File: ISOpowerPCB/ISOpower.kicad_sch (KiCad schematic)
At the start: 12 parts

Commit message: modified pcb files
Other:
- sheet MCU ports: added ADC0, ADC1, ADC2, ADC3, ADC4, ADC5; removed none

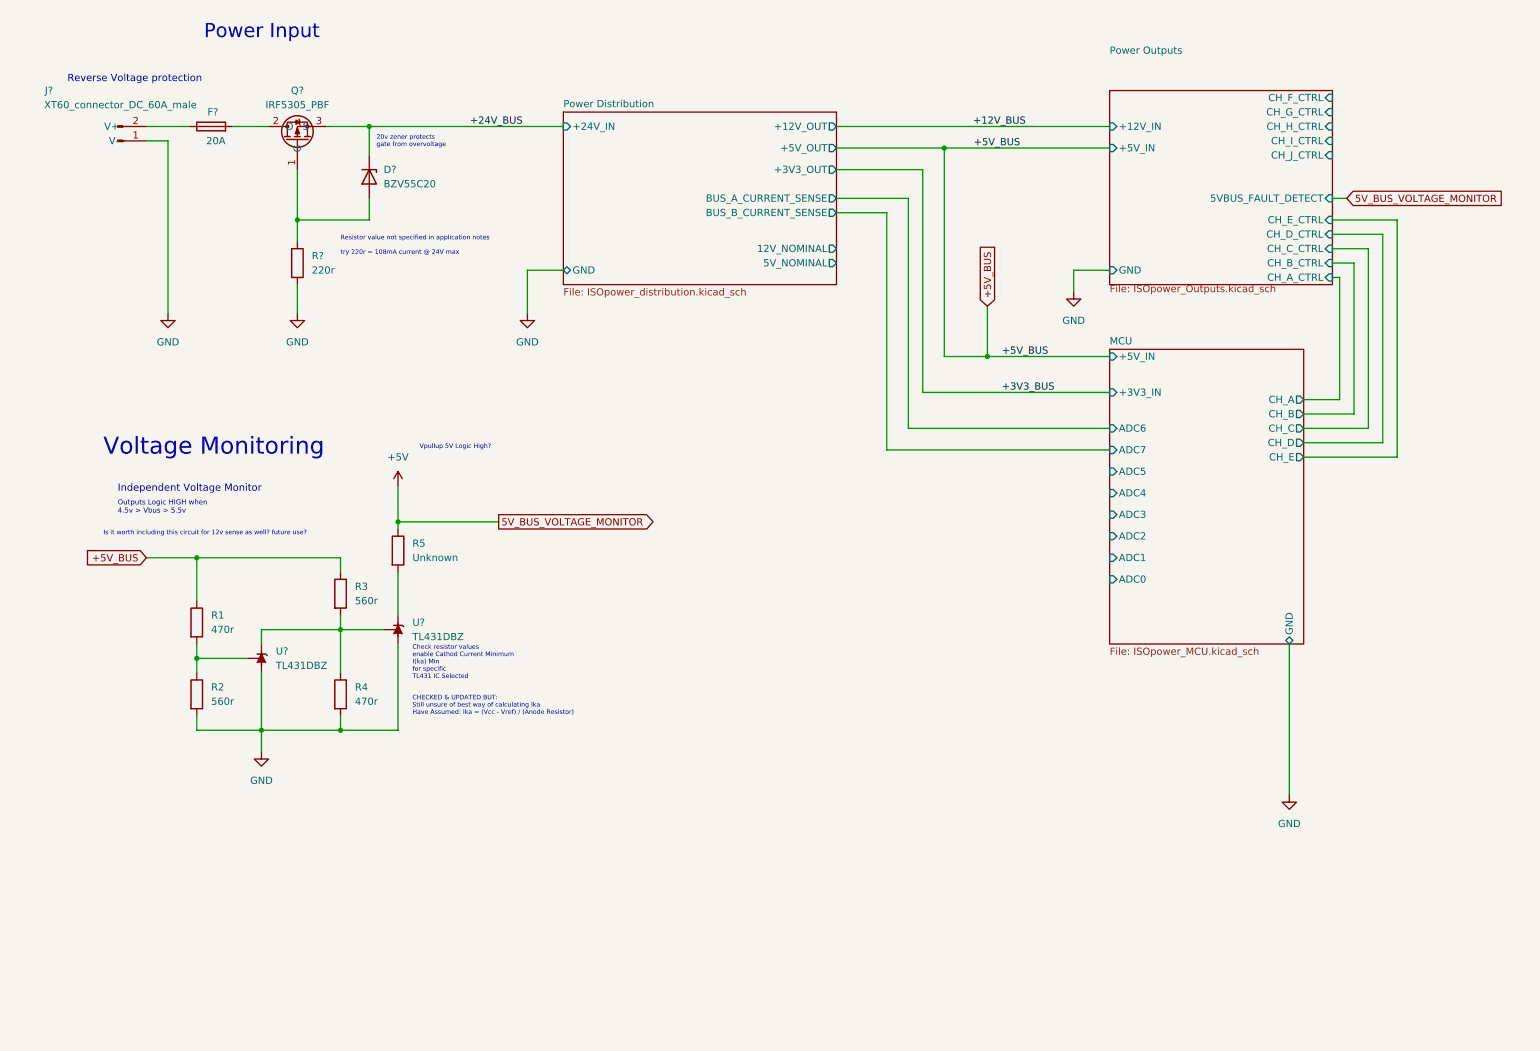
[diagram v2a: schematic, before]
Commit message: Finished initial circuit design
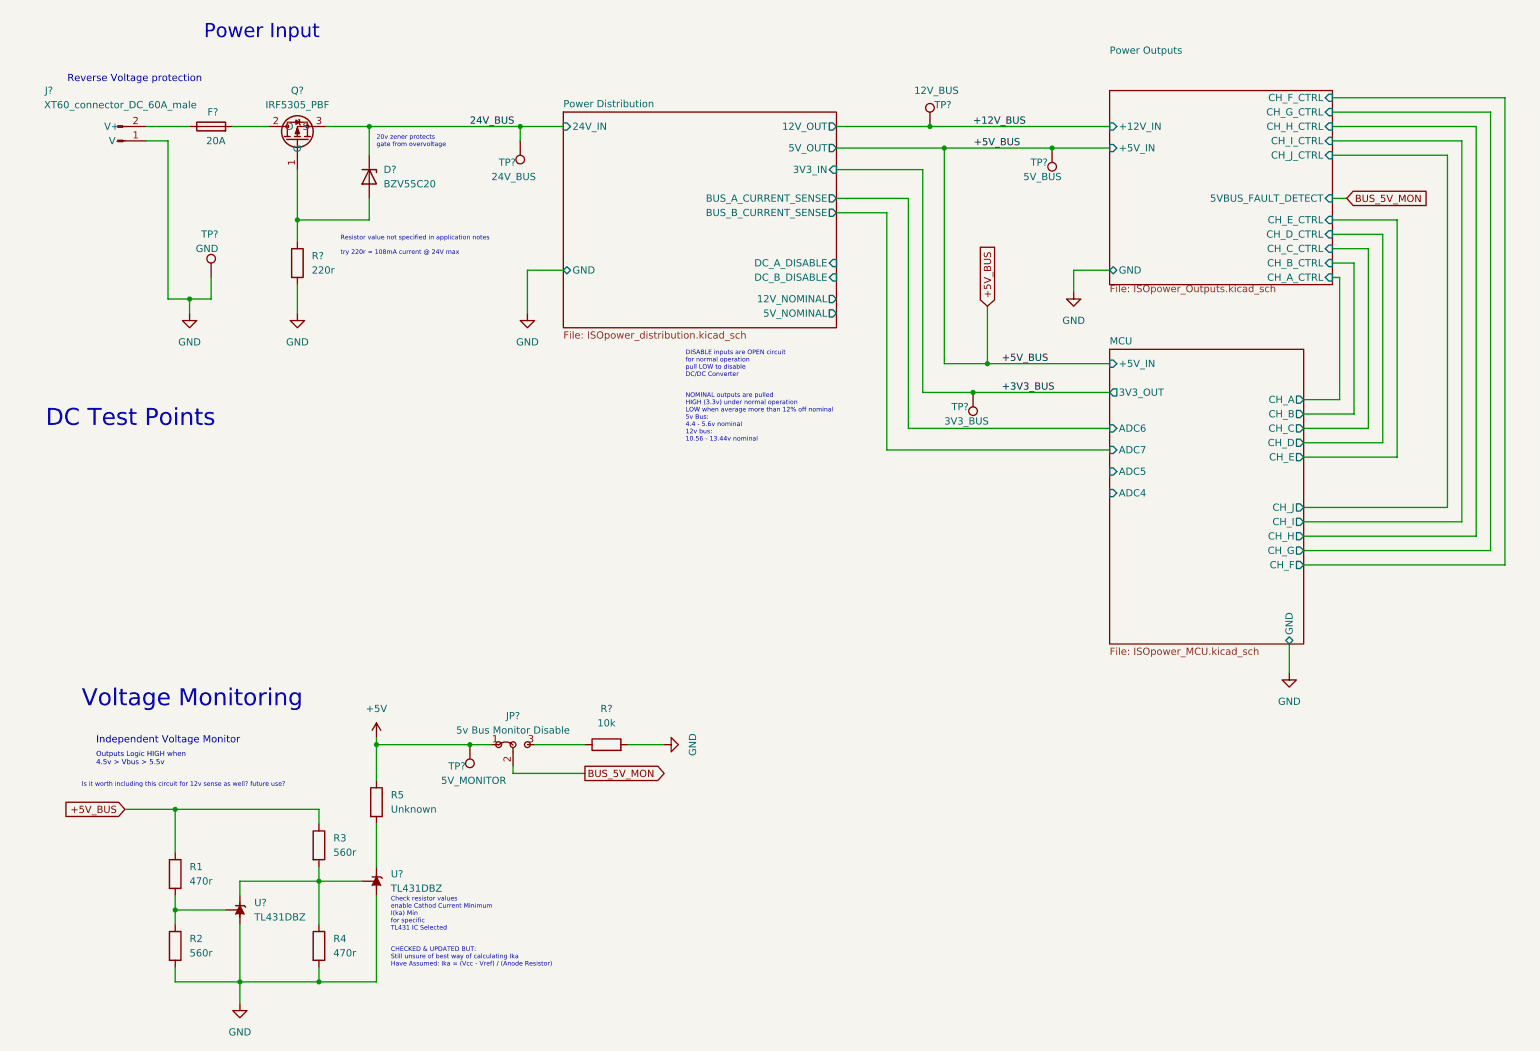
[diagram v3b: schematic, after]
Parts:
- added JP?: 5v Bus Monitor Disable, symbol 000_Connectors_Immo:Jumper_3_Bridged12
- added R?: 10k, Resistor_SMD:R_0805_2012Metric_Pad1.20x1.40mm_HandSolder, symbol 000_Resistors_Immo:Resistor_0805
- added TP?: 24V_BUS, symbol Connector:TestPoint
- added TP?: 3V3_BUS, symbol Connector:TestPoint
- added TP?: 5V_MONITOR, symbol Connector:TestPoint
- added TP?: 12V_BUS, symbol Connector:TestPoint
- added TP?: 5V_BUS, symbol Connector:TestPoint
- added TP?: GND, symbol Connector:TestPoint
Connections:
- net +12V_BUS: now also TP?.1
- net +3V3_BUS: now also TP?.1
- net +5V: now also JP?.1 (A), TP?.1
- net +5V_BUS: now also TP?.1
- net GND: now also R?.2, TP?.1
- net +24V_BUS renamed 24V_BUS
- net 24V_BUS: now also TP?.1
- new net: JP?.3 (B), R?.1
- new net BUS_5V_MON: JP?.2 (C)
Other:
- sheet MCU ports: added 3V3_OUT, CH_F, CH_G, CH_H, CH_I, CH_J; removed +3V3_IN, ADC0, ADC1, ADC2, ADC3
- sheet Power Distribution ports: added 12V_OUT, 24V_IN, 3V3_IN, 5V_OUT, DC_A_DISABLE, DC_B_DISABLE; removed +12V_OUT, +24V_IN, +3V3_OUT, +5V_OUT
- note added: "DC Test Points"
- note added: "DISABLE inputs are OPEN circuit for normal operation pull LOW to disable DC/DC Converter"
- note added: "NOMINAL outputs are pulled HIGH (3.3v) under normal operation LOW when average more than 12% off nominal 5v Bus: 4.4 - 5.6v nominal 12v bus: 10.56 - 13.44v nominal"
- note removed: "Vpullup 5V Logic High?"
- moved on the sheet: R1, R2, R3, R4, R5, U?

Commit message: PCB Notes added
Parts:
- R5: value Unknown -> 220r
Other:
- note added: "20v zener protects gate from overvoltage NOTE: check for 18v zener!"
- note added: "NOTE: 300r?"
- note removed: "20v zener protects gate from overvoltage"
- note removed: "DC Test Points"
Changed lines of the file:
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@@
     (stroke (width 0) (type default) (color 0 0 0 0))
   )
-  (wire (pts (xy 101.6 59.69) (xy 107.95 59.69))
+  (wire (pts (xy 101.6 66.04) (xy 107.95 66.04))
     (stroke (width 0) (type default) (color 0 0 0 0))
   )
@@
     (stroke (width 0) (type default) (color 0 0 0 0))
   )
+  (wire (pts (xy 101.6 69.85) (xy 101.6 66.04))
+    (stroke (width 0) (type default) (color 0 0 0 0))
+  )
   (wire (pts (xy 238.76 87.63) (xy 250.19 87.63))
     (stroke (width 0) (type default) (color 0 0 0 0))
@@
   )
   (wire (pts (xy 238.76 82.55) (xy 245.11 82.55))
-    (stroke (width 0) (type default) (color 0 0 0 0))
-  )
-  (wire (pts (xy 101.6 67.31) (xy 101.6 59.69))
     (stroke (width 0) (type default) (color 0 0 0 0))
   )
@@
     (effects (font (size 0.8 0.8)) (justify left bottom))
   )
-  (text "20v zener protects\ngate from overvoltage" (at 74.93 38.1 0)
+  (text "20v zener protects\ngate from overvoltage\n\nNOTE: \ncheck for 18v zener!"
+    (at 74.93 38.1 0)
     (effects (font (size 0.8 0.8)) (justify left bottom))
   )
-  (text "DC Test Points" (at 16.51 87.63 0)
-    (effects (font (size 3 3)) (justify left bottom))
+  (text "NOTE: 300r?\n " (at 63.5 64.77 0)
+    (effects (font (size 0.8 0.8)) (justify left bottom))
   )
   (text "CHECKED & UPDATED BUT:\nStill unsure of best way of calculating Ika\nHave Assumed: Ika = (Vcc - Vref) / (Anode Resistor)"
@@
   (symbol (lib_id "Connector:TestPoint") (at 100.33 36.83 180) (unit 1)
     (in_bom yes) (on_board yes)
-    (property "Reference" "TP?" (id 0) (at 96.52 40.64 0)
-      (effects (font (size 1.27 1.27)) (justify right))
-    )
-    (property "Value" "24V_BUS" (id 1) (at 95.25 43.18 0)
+    (property "Reference" "TP?" (id 0) (at 95.25 39.37 0)
+      (effects (font (size 1.27 1.27)) (justify right))
+    )
+    (property "Value" "24V_BUS" (id 1) (at 93.98 41.91 0)
       (effects (font (size 1.27 1.27)) (justify right))
     )
@@
       (effects (font (size 1.27 1.27)) (justify left))
     )
-    (property "Value" "Unknown" (id 1) (at 77.47 154.9399 0)
+    (property "Value" "220r" (id 1) (at 77.47 154.9399 0)
       (effects (font (size 1.27 1.27)) (justify left))
     )
@@
     (pin "1")
   )
-  (symbol (lib_id "power:GND") (at 101.6 67.31 0) (unit 1)
-    (in_bom yes) (on_board yes) (fields_autoplaced)
-    (property "Reference" "#PWR?" (id 0) (at 101.6 73.66 0)
-      (effects (font (size 1.27 1.27)) hide)
-    )
-    (property "Value" "GND" (id 1) (at 101.6 72.39 0))
-    (property "Footprint" "" (id 2) (at 101.6 67.31 0)
-      (effects (font (size 1.27 1.27)) hide)
-    )
-    (property "Datasheet" "" (id 3) (at 101.6 67.31 0)
+  (symbol (lib_id "power:GND") (at 101.6 69.85 0) (unit 1)
+    (in_bom yes) (on_board yes) (fields_autoplaced)
+    (property "Reference" "#PWR?" (id 0) (at 101.6 76.2 0)
+      (effects (font (size 1.27 1.27)) hide)
+    )
+    (property "Value" "GND" (id 1) (at 101.6 74.93 0))
+    (property "Footprint" "" (id 2) (at 101.6 69.85 0)
+      (effects (font (size 1.27 1.27)) hide)
+    )
+    (property "Datasheet" "" (id 3) (at 101.6 69.85 0)
       (effects (font (size 1.27 1.27)) hide)
     )
@@
       (effects (font (size 1.27 1.27)) (justify right))
     )
-    (pin "GND" bidirectional (at 107.95 59.69 180)
+    (pin "GND" bidirectional (at 107.95 66.04 180)
       (effects (font (size 1.27 1.27)) (justify left))
     )
@@
     )
     (path "/93c6b066-bfa2-4237-bde1-1f4f67577833"
-      (reference "R5") (unit 1) (value "Unknown") (footprint "Resistor_SMD:R_0805_2012Metric_Pad1.20x1.40mm_HandSolder")
+      (reference "R5") (unit 1) (value "220r") (footprint "Resistor_SMD:R_0805_2012Metric_Pad1.20x1.40mm_HandSolder")
     )
     (path "/1f76f9be-4bce-499b-8dda-2796b250b412/023a7f33-54b5-46cd-b7b9-89163f6e50f6"

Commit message: Major schematic revisions
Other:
- sheet Power Distribution ports: added BUS_A_DISABLE, BUS_B_DISABLE, MCU_5V_OUT; removed 12V_NOMINAL, 5V_NOMINAL, DC_A_DISABLE, DC_B_DISABLE
- sheet Power Outputs ports: added none; removed 5VBUS_FAULT_DETECT, CH_A_CTRL, CH_B_CTRL, CH_C_CTRL, CH_D_CTRL, CH_E_CTRL
- moved on the sheet: TP?

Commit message: significant changes
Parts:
- removed JP?: 5v Bus Monitor Disable, symbol 000_Connectors_Immo:Jumper_3_Bridged12
- removed R1, R4: 470r, Resistor_SMD:R_0805_2012Metric_Pad1.20x1.40mm_HandSolder, symbol 000_Resistors_Immo:Resistor_0805
- removed R2, R3: 560r, Resistor_SMD:R_0805_2012Metric_Pad1.20x1.40mm_HandSolder, symbol 000_Resistors_Immo:Resistor_0805
- removed R5: 220r, Resistor_SMD:R_0805_2012Metric_Pad1.20x1.40mm_HandSolder, symbol 000_Resistors_Immo:Resistor_0805
- removed R?: 10k, Resistor_SMD:R_0805_2012Metric_Pad1.20x1.40mm_HandSolder, symbol 000_Resistors_Immo:Resistor_0805
- removed TP?: 5V_MONITOR, symbol Connector:TestPoint
- removed U? (x2): TL431DBZ, Package_TO_SOT_SMD:SOT-23, symbol Reference_Voltage:TL431DBZ
- R?: value 220r -> 300r
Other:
- added sheet mechanical_layer (mechanical_layer.kicad_sch)
- added sheet voltage_monitoring (v_monitor.kicad_sch)
- sheet MCU ports: added IN_D, IN_E; removed CH_D, CH_E
- note added: "DISABLE inputs are CLOSED to GND for normal operation. Pull HIGH to disable DC/DC Converter."
- note added: "Still dont know what to do with BUS_5V_MON DISABLE inputs & MCU Voltage monitoring"
- note removed: "CHECKED & UPDATED BUT: Still unsure of best way of calculating Ika Have Assumed: Ika = (Vcc - Vref) / (Anode Resistor)"
- note removed: "Check resistor values enable Cathod Current Minimum I(ka) Min for specific TL431 IC Selected"
- note removed: "DISABLE inputs are OPEN circuit for normal operation pull LOW to disable DC/DC Converter"
- note removed: "Independent Voltage Monitor"
- note removed: "Is it worth including this circuit for 12v sense as well? future use?"
- note removed: "NOMINAL outputs are pulled HIGH (3.3v) under normal operation LOW when average more than 12% off nominal 5v Bus: 4.4 - 5.6v nominal 12v bus: 10.56 - 13.44v nominal"
- note removed: "Outputs Logic HIGH when 4.5v > Vbus > 5.5v"
